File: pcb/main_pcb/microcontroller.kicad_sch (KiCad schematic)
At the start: 23 parts, among them J1 Conn_01x05, J10 Conn_01x06_Male, J2 Conn_01x05, J3 Conn_01x05, J4 Conn_01x05, J5 Conn_01x05, J6 Conn_01x05, J7 Conn_01x04, J8 Conn_01x06_Male, U3 DRV8833

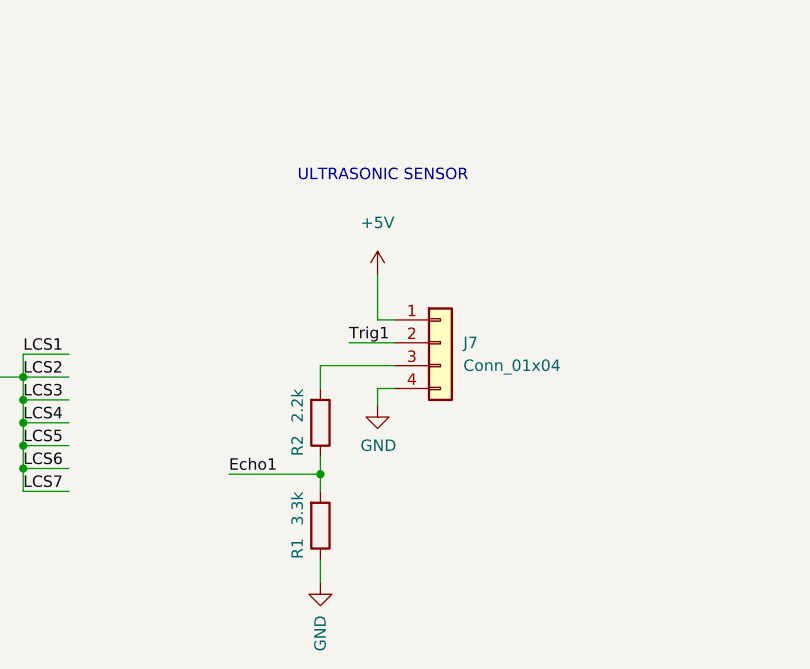
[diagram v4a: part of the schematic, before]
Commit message: deleted ultrasonic sensors
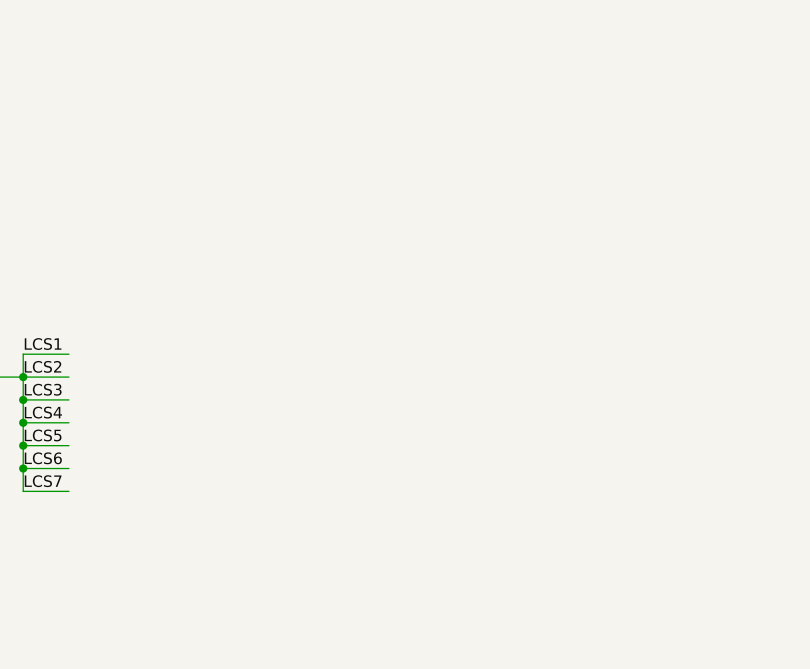
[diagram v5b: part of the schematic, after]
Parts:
- removed J7: Conn_01x04, Connector_JST:JST_XH_B4B-XH-A_1x04_P2.50mm_Vertical, symbol Connector_Generic:Conn_01x04
- removed R1: 3.3k, Resistor_SMD:R_0603_1608Metric_Pad0.98x0.95mm_HandSolder, symbol Device:R
- removed R2: 2.2k, Resistor_SMD:R_0603_1608Metric_Pad0.98x0.95mm_HandSolder, symbol Device:R
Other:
- note removed: "ULTRASONIC SENSOR"
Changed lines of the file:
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@@
   (junction (at 149.86 133.35) (diameter 0) (color 0 0 0 0)
-  )
-  (junction (at 182.88 136.525) (diameter 0) (color 0 0 0 0)
   )
   (junction (at 107.315 43.815) (diameter 0) (color 0 0 0 0)
@@
     (stroke (width 0) (type default) (color 0 0 0 0))
   )
-  (wire (pts (xy 182.88 124.46) (xy 191.135 124.46))
-    (stroke (width 0) (type default) (color 0 0 0 0))
-  )
   (wire (pts (xy 149.86 125.73) (xy 149.86 128.27))
     (stroke (width 0) (type default) (color 0 0 0 0))
@@
     (stroke (width 0) (type default) (color 0 0 0 0))
   )
-  (wire (pts (xy 189.23 128.905) (xy 189.23 127))
-    (stroke (width 0) (type default) (color 0 0 0 0))
-  )
   (wire (pts (xy 107.315 59.055) (xy 107.315 66.675))
     (stroke (width 0) (type default) (color 0 0 0 0))
@@
     (stroke (width 0) (type default) (color 0 0 0 0))
   )
-  (wire (pts (xy 189.23 127) (xy 191.135 127))
-    (stroke (width 0) (type default) (color 0 0 0 0))
-  )
   (wire (pts (xy 234.95 60.325) (xy 247.65 60.325))
     (stroke (width 0) (type default) (color 0 0 0 0))
   )
-  (wire (pts (xy 182.88 136.525) (xy 182.88 138.43))
-    (stroke (width 0) (type default) (color 0 0 0 0))
-  )
-  (wire (pts (xy 189.23 119.38) (xy 191.135 119.38))
-    (stroke (width 0) (type default) (color 0 0 0 0))
-  )
   (wire (pts (xy 246.38 45.085) (xy 246.38 55.245))
     (stroke (width 0) (type default) (color 0 0 0 0))
@@
     (stroke (width 0) (type default) (color 0 0 0 0))
   )
-  (wire (pts (xy 182.88 146.05) (xy 182.88 148.59))
-    (stroke (width 0) (type default) (color 0 0 0 0))
-  )
-  (wire (pts (xy 189.23 114.3) (xy 189.23 119.38))
-    (stroke (width 0) (type default) (color 0 0 0 0))
-  )
   (wire (pts (xy 146.685 60.325) (xy 136.525 60.325))
     (stroke (width 0) (type default) (color 0 0 0 0))
@@
     (stroke (width 0) (type default) (color 0 0 0 0))
   )
-  (wire (pts (xy 172.72 136.525) (xy 182.88 136.525))
-    (stroke (width 0) (type default) (color 0 0 0 0))
-  )
-  (wire (pts (xy 182.88 134.62) (xy 182.88 136.525))
-    (stroke (width 0) (type default) (color 0 0 0 0))
-  )
   (wire (pts (xy 93.345 43.815) (xy 96.52 43.815))
     (stroke (width 0) (type default) (color 0 0 0 0))
@@
     (stroke (width 0) (type default) (color 0 0 0 0))
   )
-  (wire (pts (xy 186.055 121.92) (xy 191.135 121.92))
-    (stroke (width 0) (type default) (color 0 0 0 0))
-  )
   (wire (pts (xy 35.56 48.26) (xy 48.26 48.26))
-    (stroke (width 0) (type default) (color 0 0 0 0))
-  )
-  (wire (pts (xy 182.88 127) (xy 182.88 124.46))
     (stroke (width 0) (type default) (color 0 0 0 0))
   )
@@
     (effects (font (size 5.08 5.08)) (justify left bottom))
   )
-  (text "ULTRASONIC SENSOR" (at 180.34 104.14 0)
-    (effects (font (size 1.27 1.27)) (justify left bottom))
-  )
   (label "LED3" (at 129.54 125.73 0)
     (effects (font (size 1.27 1.27)) (justify left bottom))
@@
     (effects (font (size 1.27 1.27)) (justify left bottom))
   )
-  (label "Echo1" (at 172.72 136.525 0)
-    (effects (font (size 1.27 1.27)) (justify left bottom))
-  )
   (label "LCS7" (at 48.26 124.46 180)
     (effects (font (size 1.27 1.27)) (justify right bottom))
@@
   )
   (label "LED1" (at 73.025 43.815 0)
-    (effects (font (size 1.27 1.27)) (justify left bottom))
-  )
-  (label "Trig1" (at 186.055 121.92 0)
     (effects (font (size 1.27 1.27)) (justify left bottom))
   )
@@
     (pin "2")
   )
-  (symbol (lib_id "power:GND") (at 182.88 148.59 0) (unit 1)
-    (in_bom yes) (on_board yes)
-    (property "Reference" "#PWR019" (id 0) (at 182.88 154.94 0)
-      (effects (font (size 1.27 1.27)) hide)
-    )
-    (property "Value" "GND" (id 1) (at 182.88 156.21 90)
-      (effects (font (size 1.27 1.27)) (justify left))
-    )
-    (property "Footprint" "" (id 2) (at 182.88 148.59 0)
-      (effects (font (size 1.27 1.27)) hide)
-    )
-    (property "Datasheet" "" (id 3) (at 182.88 148.59 0)
-      (effects (font (size 1.27 1.27)) hide)
-    )
-    (pin "1")
-  )
   (symbol (lib_id "Device:R") (at 100.33 59.055 270) (unit 1)
     (in_bom yes) (on_board yes)
@@
     )
     (property "Datasheet" "~" (id 3) (at 100.33 59.055 0)
-      (effects (font (size 1.27 1.27)) hide)
-    )
-    (pin "1")
-    (pin "2")
-  )
-  (symbol (lib_id "Device:R") (at 182.88 142.24 0) (mirror x) (unit 1)
-    (in_bom yes) (on_board yes)
-    (property "Reference" "R1" (id 0) (at 180.34 144.78 90))
-    (property "Value" "3.3k" (id 1) (at 180.34 140.335 90))
-    (property "Footprint" "Resistor_SMD:R_0603_1608Metric_Pad0.98x0.95mm_HandSolder" (id 2) (at 181.102 142.24 90)
-      (effects (font (size 1.27 1.27)) hide)
-    )
-    (property "Datasheet" "~" (id 3) (at 182.88 142.24 0)
       (effects (font (size 1.27 1.27)) hide)
     )
@@
     (pin "1")
   )
-  (symbol (lib_id "power:GND") (at 189.23 128.905 0) (unit 1)
-    (in_bom yes) (on_board yes)
-    (property "Reference" "#PWR021" (id 0) (at 189.23 135.255 0)
-      (effects (font (size 1.27 1.27)) hide)
-    )
-    (property "Value" "GND" (id 1) (at 187.325 133.35 0)
-      (effects (font (size 1.27 1.27)) (justify left))
-    )
-    (property "Footprint" "" (id 2) (at 189.23 128.905 0)
-      (effects (font (size 1.27 1.27)) hide)
-    )
-    (property "Datasheet" "" (id 3) (at 189.23 128.905 0)
-      (effects (font (size 1.27 1.27)) hide)
-    )
-    (pin "1")
-  )
   (symbol (lib_id "power:+3V3") (at 35.56 127 270) (unit 1)
     (in_bom yes) (on_board yes) (fields_autoplaced)
@@
     (pin "6")
   )
-  (symbol (lib_id "power:+5V") (at 189.23 114.3 0) (unit 1)
-    (in_bom yes) (on_board yes) (fields_autoplaced)
-    (property "Reference" "#PWR020" (id 0) (at 189.23 118.11 0)
-      (effects (font (size 1.27 1.27)) hide)
-    )
-    (property "Value" "+5V" (id 1) (at 189.23 108.585 0))
-    (property "Footprint" "" (id 2) (at 189.23 114.3 0)
-      (effects (font (size 1.27 1.27)) hide)
-    )
-    (property "Datasheet" "" (id 3) (at 189.23 114.3 0)
-      (effects (font (size 1.27 1.27)) hide)
-    )
-    (pin "1")
-  )
   (symbol (lib_id "power:+3V3") (at 35.56 55.88 270) (unit 1)
     (in_bom yes) (on_board yes) (fields_autoplaced)
@@
     )
     (pin "1")
-  )
-  (symbol (lib_id "Connector_Generic:Conn_01x04") (at 196.215 121.92 0) (unit 1)
-    (in_bom yes) (on_board yes) (fields_autoplaced)
-    (property "Reference" "J7" (id 0) (at 198.755 121.9199 0)
-      (effects (font (size 1.27 1.27)) (justify left))
-    )
-    (property "Value" "Conn_01x04" (id 1) (at 198.755 124.4599 0)
-      (effects (font (size 1.27 1.27)) (justify left))
-    )
-    (property "Footprint" "Connector_JST:JST_XH_B4B-XH-A_1x04_P2.50mm_Vertical" (id 2) (at 196.215 121.92 0)
-      (effects (font (size 1.27 1.27)) hide)
-    )
-    (property "Datasheet" "~" (id 3) (at 196.215 121.92 0)
-      (effects (font (size 1.27 1.27)) hide)
-    )
-    (pin "1")
-    (pin "2")
-    (pin "3")
-    (pin "4")
   )
   (symbol (lib_id "Connector_Generic:Conn_01x05") (at 30.48 106.68 0) (mirror y) (unit 1)
@@
       (effects (font (size 1.27 1.27)) hide)
     )
-    (pin "1")
-    (pin "2")
-  )
-  (symbol (lib_id "Device:R") (at 182.88 130.81 0) (mirror x) (unit 1)
-    (in_bom yes) (on_board yes)
-    (property "Reference" "R2" (id 0) (at 180.34 133.35 90))
-    (property "Value" "2.2k" (id 1) (at 180.34 128.905 90))
-    (property "Footprint" "Resistor_SMD:R_0603_1608Metric_Pad0.98x0.95mm_HandSolder" (id 2) (at 181.102 130.81 90)
-      (effects (font (size 1.27 1.27)) hide)
-    )
-    (property "Datasheet" "~" (id 3) (at 182.88 130.81 0)
-      (effects (font (size 1.27 1.27)) hide)
-    )
